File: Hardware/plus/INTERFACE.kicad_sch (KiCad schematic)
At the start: 62 parts, among them J3 Conn_ARM_JTAG_SWD_20, J5 WAFER-ZH1.5-4PWB, Q1 SI2305, U10 SN74LVC1G125DCK, U11 SN74LVC1G125DCK, U12 SN74LVC2T45DCUR, U13 SN74LVC2T45DCUR, U14 ADS1115IDGS, U15 LMV358, U3 SN74LVC1G125DCK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

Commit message: 修正串口线序
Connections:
- net GND: now also J5.4 (Pin_4); no longer J5.1 (Pin_1)
- net UART_RX: now also J5.3 (Pin_3); no longer J5.2 (Pin_2)
- net UART_TX: now also J5.2 (Pin_2); no longer J5.3 (Pin_3)
- net VTREF: now also J5.1 (Pin_1); no longer J5.4 (Pin_4)
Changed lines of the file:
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@@
 	)
 	(junction
+		(at 267.97 129.54)
+		(diameter 0)
+		(color 0 0 0 0)
+	)
+	(junction
 		(at 245.11 144.78)
 		(diameter 0)
@@
 	(wire
 		(pts
-			(xy 254 124.46) (xy 262.89 124.46)
-		)
-		(stroke
-			(width 0)
-			(type default)
-		)
-	)
-	(wire
-		(pts
 			(xy 48.26 76.2) (xy 48.26 81.28)
 		)
@@
 	(wire
 		(pts
+			(xy 262.89 124.46) (xy 262.89 129.54)
+		)
+		(stroke
+			(width 0)
+			(type default)
+		)
+	)
+	(wire
+		(pts
 			(xy 146.05 176.53) (xy 146.05 172.72)
 		)
@@
 	(wire
 		(pts
+			(xy 262.89 129.54) (xy 267.97 129.54)
+		)
+		(stroke
+			(width 0)
+			(type default)
+		)
+	)
+	(wire
+		(pts
 			(xy 246.38 33.02) (xy 254 33.02)
 		)
@@
 	)
 	(label "UART_RX"
-		(at 254 119.38 0)
+		(at 254 121.92 0)
 		(effects
 			(font
@@
 	)
 	(label "UART_TX"
-		(at 254 121.92 0)
+		(at 254 119.38 0)
 		(effects
 			(font
@@
 	)
 	(symbol
-		(lib_id "power:GND")
-		(at 254 116.84 270)
-		(unit 1)
-		(exclude_from_sim no)
-		(in_bom yes)
-		(on_board yes)
-		(dnp no)
-		(fields_autoplaced yes)
-		(property "Reference" "#PWR0114"
-			(at 247.65 116.84 0)
-			(effects
-				(font
-					(size 1.27 1.27)
-				)
-				(hide yes)
-			)
-		)
-		(property "Value" "GND"
-			(at 250.19 116.8399 90)
-			(effects
-				(font
-					(size 1.27 1.27)
-				)
-				(justify right)
-			)
-		)
-		(property "Footprint" ""
-			(at 254 116.84 0)
-			(effects
-				(font
-					(size 1.27 1.27)
-				)
-				(hide yes)
-			)
-		)
-		(property "Datasheet" ""
-			(at 254 116.84 0)
-			(effects
-				(font
-					(size 1.27 1.27)
-				)
-				(hide yes)
-			)
-		)
-		(property "Description" "Power symbol creates a global label with name \"GND\" , ground"
-			(at 254 116.84 0)
-			(effects
-				(font
-					(size 1.27 1.27)
-				)
-				(hide yes)
-			)
-		)
-		(pin "1"
-		)
-		(instances
-			(project "HFLink_Plus"
-				(path "/3baf7474-83dc-4d17-85a7-862b5853a92a/486eb215-8ff5-4def-8b9d-57fcc34d9fbf"
-					(reference "#PWR0114")
-					(unit 1)
-				)
-			)
-		)
-	)
-	(symbol
 		(lib_id "HPM6280Foc:0402WGF4701TCE")
 		(at 224.79 34.29 90)
@@
 	(symbol
 		(lib_id "power:+1V0")
-		(at 254 124.46 90)
+		(at 254 116.84 90)
 		(unit 1)
 		(exclude_from_sim no)
@@
 		(fields_autoplaced yes)
 		(property "Reference" "#PWR0115"
-			(at 257.81 124.46 0)
+			(at 257.81 116.84 0)
 			(effects
 				(font
@@
 		)
 		(property "Value" "VTREF"
-			(at 250.19 124.4599 90)
+			(at 250.19 116.8399 90)
 			(effects
 				(font
@@
 		)
 		(property "Footprint" ""
-			(at 254 124.46 0)
+			(at 254 116.84 0)
 			(effects
 				(font
@@
 		)
 		(property "Datasheet" ""
-			(at 254 124.46 0)
+			(at 254 116.84 0)
 			(effects
 				(font
@@
 		)
 		(property "Description" "Power symbol creates a global label with name \"+1V0\""
-			(at 254 124.46 0)
+			(at 254 116.84 0)
 			(effects
 				(font

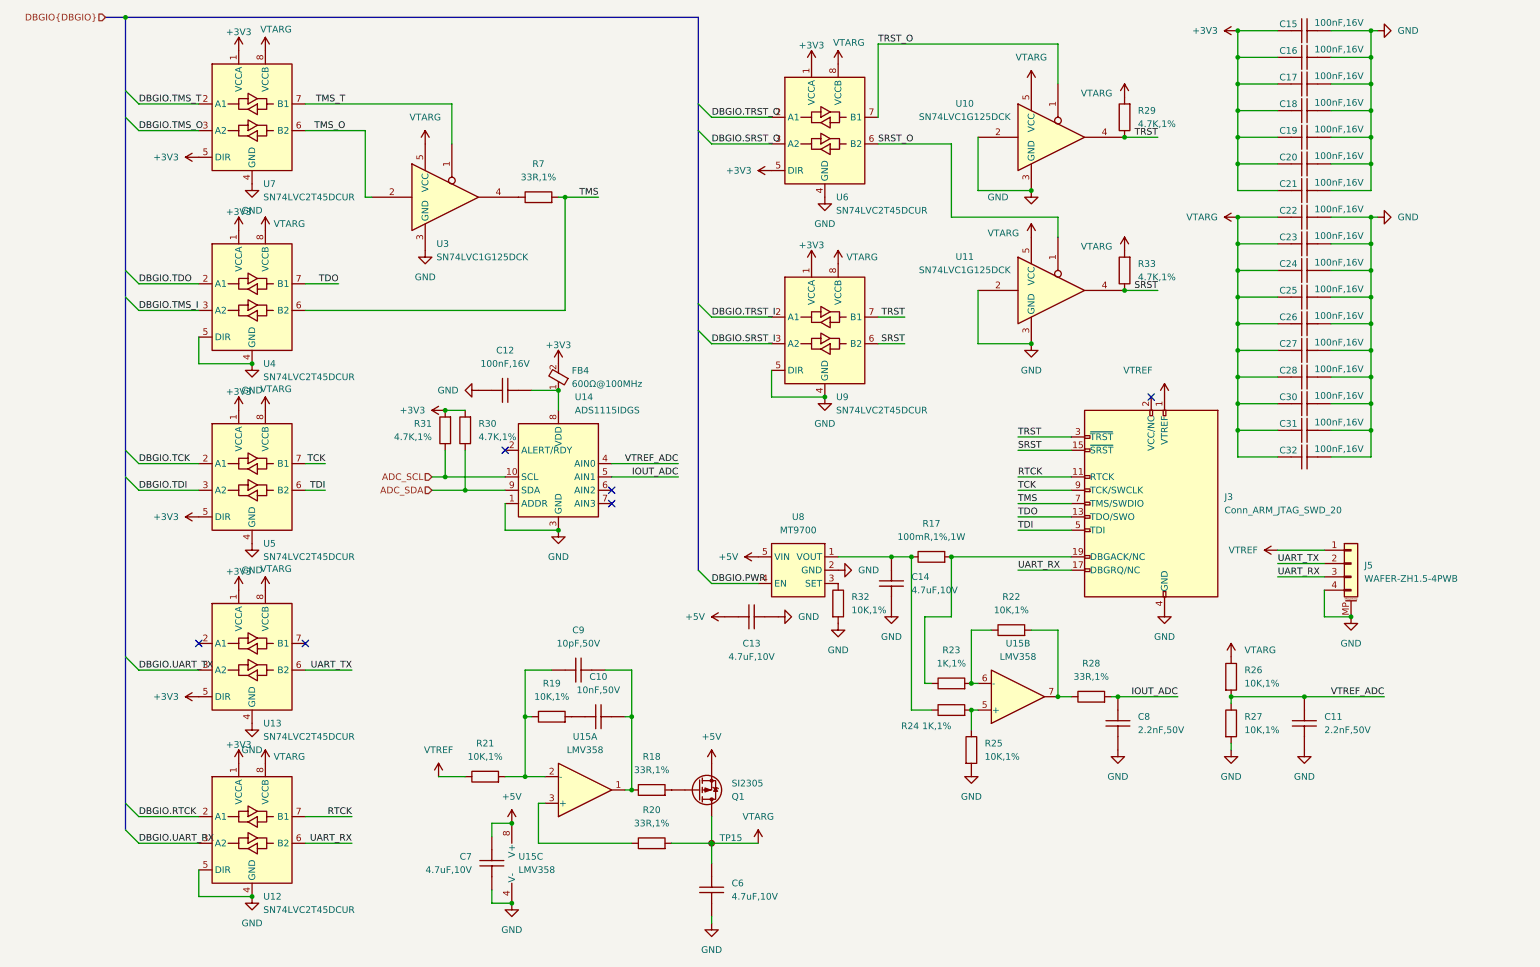
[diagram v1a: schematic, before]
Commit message: 移植到新硬件
【PCB】输出端口串联33欧电阻，螺丝孔接地，串口RX上拉
【RTL】引脚适配，重构GPIO
【MCU】支持1115读取电压电流
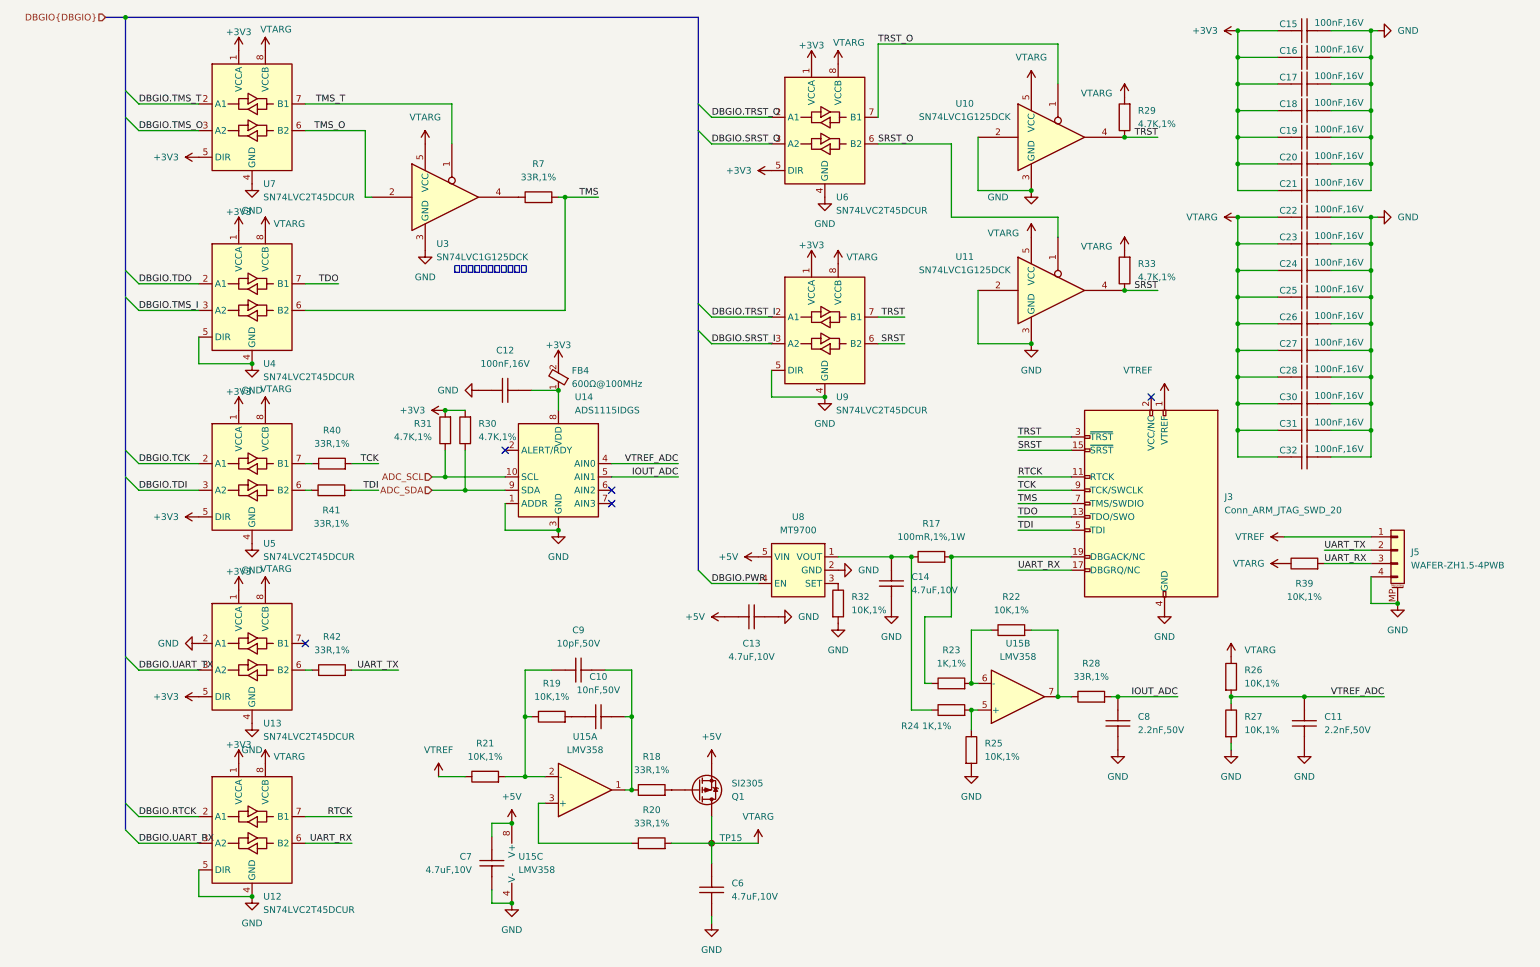
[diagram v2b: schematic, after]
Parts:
- added R39: 10K,1%, Resistor_SMD:R_0402_1005Metric, symbol HPM6280Foc:0402WGF1002TCE
- added R40, R41, R42: 33R,1%, Resistor_SMD:R_0402_1005Metric, symbol HPM6280Foc:0402WGF330JTCE
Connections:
- net GND: now also U13.2 (A1)
- net TCK: now also R40.2; no longer U5.7 (B1)
- net TDI: now also R41.2; no longer U5.6 (B2)
- net UART_RX: now also R39.2
- net UART_TX: now also R42.2; no longer U13.6 (B2)
- net VTARG: now also R39.1
- new net: R41.1, U5.6 (B2)
- new net: R40.1, U5.7 (B1)
- new net: R42.1, U13.6 (B2)
- no-connect marks 6 -> 5
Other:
- note added: "延迟敏感，不要买友台的"
- moved on the sheet: J5

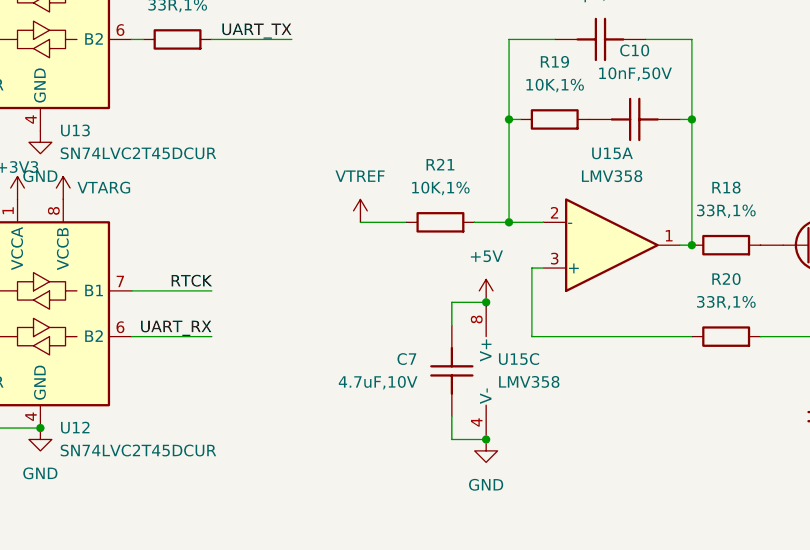
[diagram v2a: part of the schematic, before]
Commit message: [PCB] vtrg增加100K下拉电阻
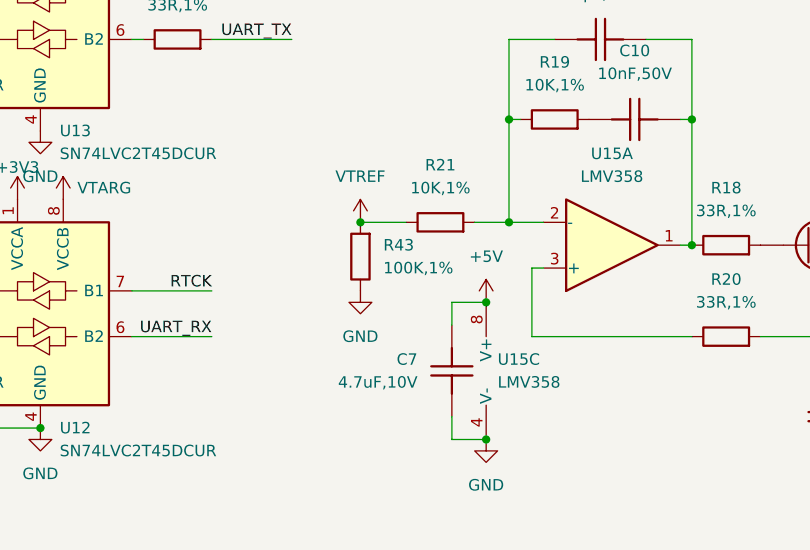
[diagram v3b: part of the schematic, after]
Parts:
- added R43: 100K,1%, Resistor_SMD:R_0402_1005Metric, symbol HPM6280Foc:RC0402FR-0710KL
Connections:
- net GND: now also R43.1
- net VTREF: now also R43.2
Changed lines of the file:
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@@
 	)
 	(junction
+		(at 93.98 160.02)
+		(diameter 0)
+		(color 0 0 0 0)
+	)
+	(junction
 		(at 191.77 118.11)
 		(diameter 0)
@@
 	)
 	(symbol
+		(lib_id "HPM6280Foc:RC0402FR-0710KL")
+		(at 93.98 163.83 90)
+		(unit 1)
+		(exclude_from_sim no)
+		(in_bom yes)
+		(on_board yes)
+		(dnp no)
+		(fields_autoplaced yes)
+		(property "Reference" "R43"
+			(at 96.52 162.5599 90)
+			(effects
+				(font
+					(size 1.27 1.27)
+				)
+				(justify right)
+			)
+		)
+		(property "Value" "100K,1%"
+			(at 96.52 165.0999 90)
+			(effects
+				(font
+					(size 1.27 1.27)
+				)
+				(justify right)
+			)
+		)
+		(property "Footprint" "Resistor_SMD:R_0402_1005Metric"
+			(at 93.98 163.83 0)
+			(effects
+				(font
+					(size 1.27 1.27)
+				)
+				(hide yes)
+			)
+		)
+		(property "Datasheet" ""
+			(at 93.98 163.83 0)
+			(effects
+				(font
+					(size 1.27 1.27)
+				)
+				(hide yes)
+			)
+		)
+		(property "Description" ""
+			(at 93.98 163.83 0)
+			(effects
+				(font
+					(size 1.27 1.27)
+				)
+				(hide yes)
+			)
+		)
+		(property "华秋编号" "G0038899"
+			(at 93.98 163.83 0)
+			(effects
+				(font
+					(size 1.27 1.27)
+				)
+				(hide yes)
+			)
+		)
+		(property "立创编号" "C60491"
+			(at 97.79 167.64 0)
+			(effects
+				(font
+					(size 1.27 1.27)
+				)
+				(hide yes)
+			)
+		)
+		(property "制造商" "YAGEO(国巨)"
+			(at 93.98 163.83 0)
+			(effects
+				(font
+					(size 1.27 1.27)
+				)
+				(hide yes)
+			)
+		)
+		(pin "2"
+		)
+		(pin "1"
+		)
+		(instances
+			(project ""
+				(path "/3baf7474-83dc-4d17-85a7-862b5853a92a/486eb215-8ff5-4def-8b9d-57fcc34d9fbf"
+					(reference "R43")
+					(unit 1)
+				)
+			)
+		)
+	)
+	(symbol
 		(lib_id "power:GND")
 		(at 58.42 115.57 0)
@@
 					(unit 1)
 				)
+			)
+		)
+	)
+	(symbol
+		(lib_id "power:GND")
+		(at 93.98 167.64 0)
+		(unit 1)
+		(exclude_from_sim no)
+		(in_bom yes)
+		(on_board yes)
+		(dnp no)
+		(fields_autoplaced yes)
+		(property "Reference" "#PWR0118"
+			(at 93.98 173.99 0)
+			(effects
+				(font
+					(size 1.27 1.27)
+				)
+				(hide yes)
+			)
+		)
+		(property "Value" "GND"
+			(at 93.98 172.72 0)
+			(effects
+				(font
+					(size 1.27 1.27)
+				)
+			)
+		)
+		(property "Footprint" ""
+			(at 93.98 167.64 0)
+			(effects
+				(font
+					(size 1.27 1.27)
+				)
+				(hide yes)
+			)
+		)
+		(property "Datasheet" ""
+			(at 93.98 167.64 0)
+			(effects
+				(font
+					(size 1.27 1.27)
+				)
+				(hide yes)
+			)
+		)
+		(property "Description" "Power symbol creates a global label with name \"GND\" , ground"
+			(at 93.98 167.64 0)
+			(effects
+				(font
+					(size 1.27 1.27)
+				)
+				(hide yes)
+			)
+		)
+		(pin "1"
+		)
+		(instances
+			(project "HFLink_Plus"
+				(path "/3baf7474-83dc-4d17-85a7-862b5853a92a/486eb215-8ff5-4def-8b9d-57fcc34d9fbf"
+					(reference "#PWR0118")
+					(unit 1)
+				)

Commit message: PCB JTAG每个信号都增加33欧串阻，USB供电电压传感
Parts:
- added C33: 2.2nF,50V, Capacitor_SMD:C_0402_1005Metric, symbol HPM6280Foc:0402B222K500NT
- added R44, R45, R46: 33R,1%, Resistor_SMD:R_0402_1005Metric, symbol HPM6280Foc:0402WGF330JTCE
- added R47, R48: 10K,1%, Resistor_SMD:R_0402_1005Metric, symbol HPM6280Foc:0402WGF1002TCE
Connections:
- net +5V: now also R47.1
- net GND: now also C33.2, R48.2
- net RTCK: now also R44.2; no longer U12.7 (B1)
- net TDO: now also R46.2; no longer U4.7 (B1)
- net TMS: no longer U4.6 (B2)
- net UART_RX: now also R45.2; no longer U12.6 (B2)
- net at R7.1, U3.4: now also U4.6 (B2)
- net VBUS_ADC: now reaches U14.6 (AIN2)
- net VBUS_ADC: now also C33.1, R47.2, R48.1
- new net: R44.1, U12.7 (B1)
- new net: R46.1, U4.7 (B1)
- new net: R45.1, U12.6 (B2)
- no-connect marks 5 -> 4
